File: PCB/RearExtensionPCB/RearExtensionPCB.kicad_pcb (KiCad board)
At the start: 2 copper layers, 3 parts, among them J1 Conn_01x10, SW1 RotaryEncoder_Switch, U1 ER_OLEDM0.91_1x-I2C

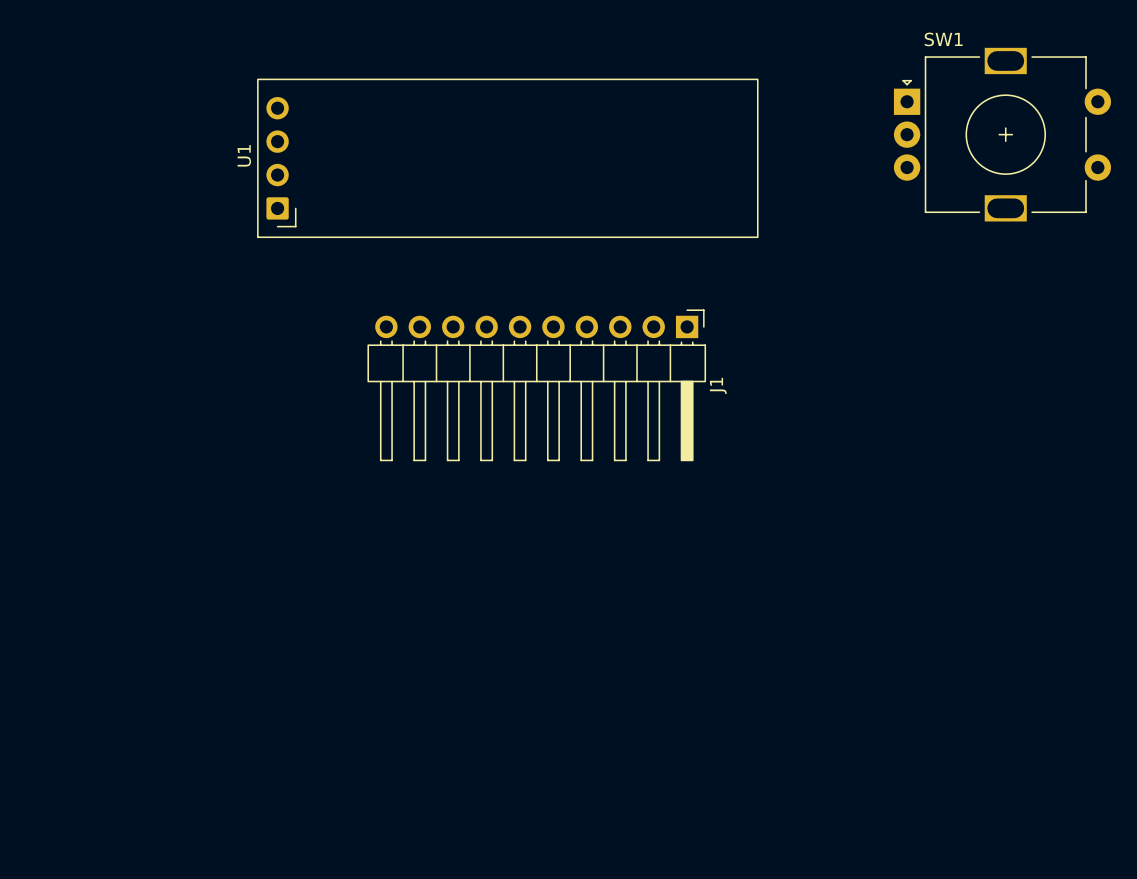
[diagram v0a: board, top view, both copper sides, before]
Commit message: Finished Rear Extention and added 3D Models
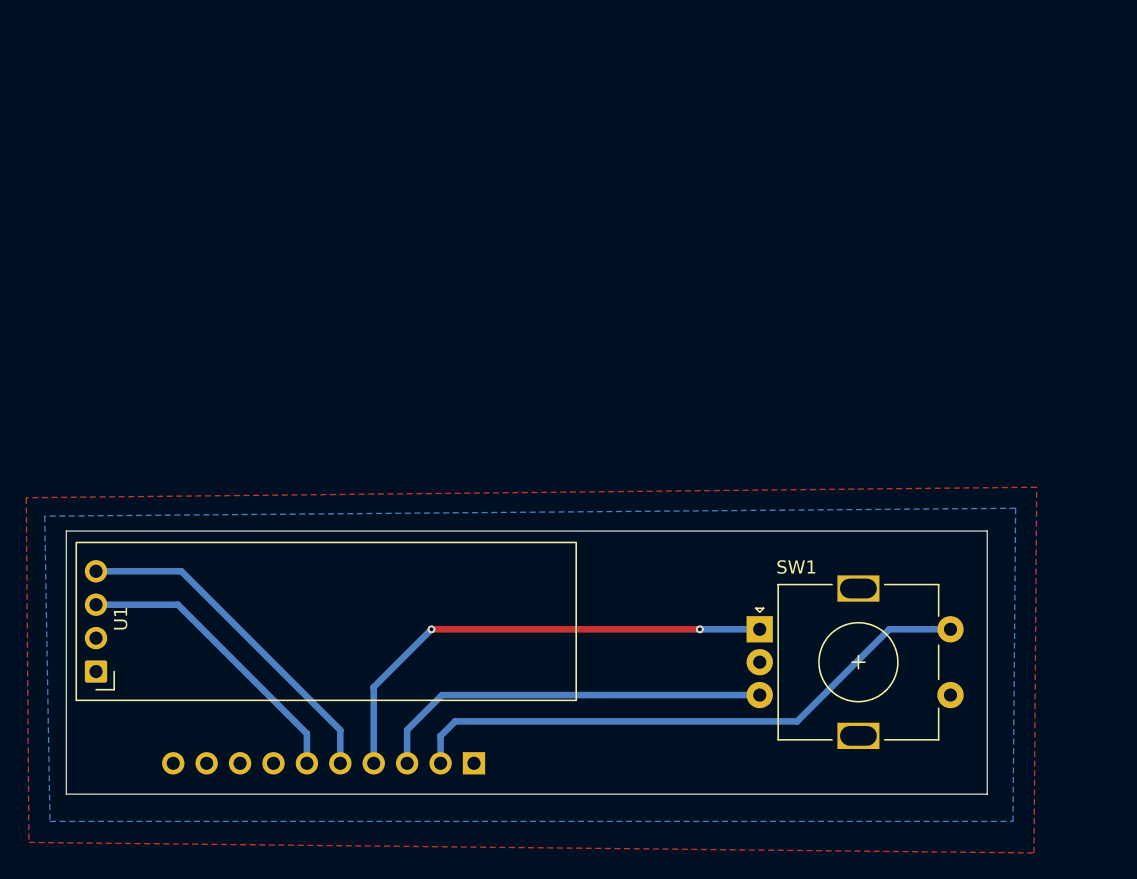
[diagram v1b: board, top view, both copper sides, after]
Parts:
- J1: moved to B.Cu
- moved SW1 41.6 mm to (172.8, 102.6)
- moved U1 37.8 mm to (122.3, 105.8)
- moved J1 36.9 mm to (151.0, 112.8), turned to 90 degrees
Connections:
- J1 pad 2: Rotary A -> Rotary Switch
- J1 pad 4: Rotary Switch -> Rotary A
- J1 pad 5: OLED SCL -> OLED SDA
- J1 pad 6: OLED SDA -> OLED SCL
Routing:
- net Rotary Switch: track 0.00 -> 44.2 mm
- net Rotary A: track 0.00 -> 37.0 mm, vias 0 -> 2
- net Rotary B: track 0.00 -> 30.4 mm
- net OLED SDA: track 0.00 -> 26.1 mm
- net OLED SCL: track 0.00 -> 22.3 mm
- added copper zone on B.Cu, net GND
- added copper zone on F.Cu, net VBUS
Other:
- board outline added: 70 x 20 mm
- board text added: "GND"
- board text added: "OLED SCL"
- board text added: "OLED SDA"
- board text added: "Rot A"
- board text added: "Rot B"
- board text added: "Rot Sw"
- board text added: "VBUS"
